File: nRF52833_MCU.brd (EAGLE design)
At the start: 36.3 x 28.4 mm, 20 parts, among them IC1 SKY13415-485LF, IC2 BQ25570RGRR, J100 DEBUG_CONNECTOR, X1 32MHz, X2 32.768kHz

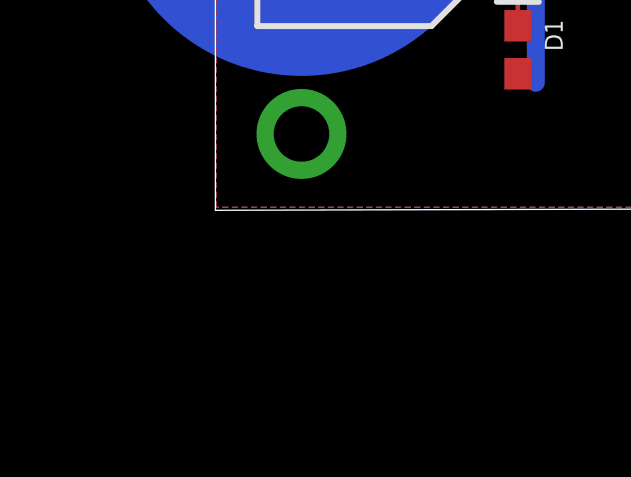
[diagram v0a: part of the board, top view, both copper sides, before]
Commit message: Add gpios for nrf52833
Signed-off-by: Florian Depraz <florian.depraz@outlook.com>
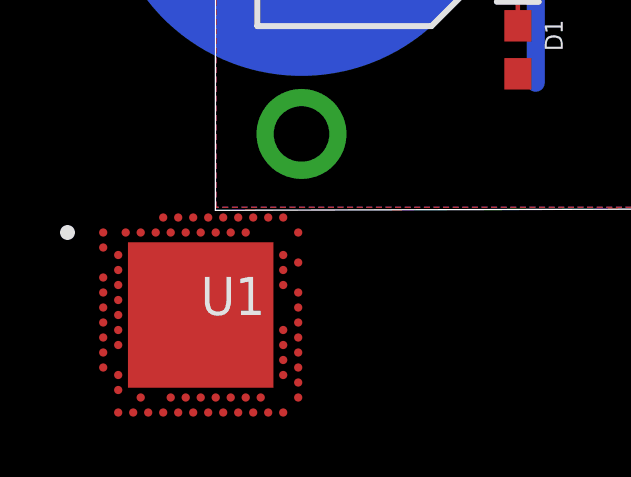
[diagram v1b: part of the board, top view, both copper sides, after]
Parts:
- added U1: nRF52833-QIAA, nrf52833_qiaa:AQFN50P700X700X85_HS-74N
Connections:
- removed net AC31/RESET: J100.10
- removed net P0.19_TX: J100.8
- removed net P0.20_RX: J100.7
- new net DEC1: U1.C1
- new net DEC3: U1.D23
- new net DEC4: U1.B5
- new net DEC5: U1.N24
- new net DEC6: U1.E24
- new net DECUSB: U1.AC5
- new net P0.06_TX: J100.8, U1.L1
- new net P0.07_RX: J100.7, U1.M2
- new net RESET: J100.10, U1.AC13
- new net VBUS: U1.AD2
- new net VDD: U1.A22, U1.AD14, U1.AD23, U1.B1, U1.W1
- new net VDDH: U1.Y2
- new net VSS: U1.74, U1.B7
- new net VSS_PA: U1.F23
- net ANT: now also U1.H23
- net ANT_SEL_V1: now also U1.U24
- net ANT_SEL_V2: now also U1.R24
- net ANT_SEL_V3: now also U1.P23
- net N$3: now also U1.A23
- net N$37: now also U1.B24
- net N$38: now also U1.D2
- net N$39: now also U1.F2
- net P0.21_LED: now also U1.AC17
- net SWDCLK: now also U1.AA24
- net SWDIO: now also U1.AC24
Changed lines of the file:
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@@
 <attribute name="VALUE" x="7.34" y="22.84" size="1.27" layer="27" align="center"/>
+</element>
+<element name="U1" library="nrf52833_qiaa" package="AQFN50P700X700X85_HS-74N" value="nRF52833-QIAA" x="-1.56" y="-3.59" smashed="yes">
+<attribute name="ASSEMBLY" value="" x="-1.56" y="-3.59" size="1.778" layer="27" display="off"/>
+<attribute name="FOOTPRINT_DOC" value="AQFN-73" x="-1.56" y="-3.59" size="1.778" layer="27" display="off"/>
+<attribute name="LATESTREVISIONDATE" value="2018-12-03" x="-1.56" y="-3.59" size="1.778" layer="27" display="off"/>
+<attribute name="MANUFACTURER" value="Nordic Semiconductor" x="-1.56" y="-3.59" size="1.778" layer="27" display="off"/>
+<attribute name="MANUFACTURER_PART_NUMBER" value="nRF52833-QIAA" x="-1.56" y="-3.59" size="1.778" layer="27" display="off"/>
+<attribute name="NAME" x="-1.56" y="-3.59" size="1.27" layer="25" font="vector"/>
+<attribute name="NOTE" value="*" x="-1.56" y="-3.59" size="1.778" layer="27" display="off"/>
+<attribute name="PART_NUMBER" value="nRF52833-QIAA" x="-1.56" y="-3.59" size="1.778" layer="27" display="off"/>
+<attribute name="PIN_COUNT" value="73" x="-1.56" y="-3.59" size="1.778" layer="27" display="off"/>
+<attribute name="PUBLISHED" value="2018-12-03" x="-1.56" y="-3.59" size="1.778" layer="27" display="off"/>
+<attribute name="PUBLISHER" value="Nordic Semiconductor" x="-1.56" y="-3.59" size="1.778" layer="27" display="off"/>
+<attribute name="VALUE" x="-1.56" y="-5.114" size="1.27" layer="27" font="vector"/>
 </element>
 </elements>
@@
 <signal name="ANT">
 <contactref element="IC1" pad="13"/>
-</signal>
-<signal name="P0.19_TX">
+<contactref element="U1" pad="H23"/>
+<wire x1="1.190003125" y1="-2.590003125" x2="18.507" y2="11.12" width="0" layer="19" extent="1-1"/>
+</signal>
+<signal name="P0.06_TX">
 <contactref element="J100" pad="8"/>
+<contactref element="U1" pad="L1"/>
+<wire x1="-4.81" y1="-3.34" x2="1.78" y2="12.31" width="0" layer="19" extent="1-1"/>
 </signal>
 <signal name="P0.21_LED">
 <contactref element="R5" pad="1"/>
-</signal>
-<signal name="P0.20_RX">
+<contactref element="U1" pad="AC17"/>
+<wire x1="-0.56" y1="-6.340003125" x2="9.01" y2="8.6" width="0" layer="19" extent="1-1"/>
+</signal>
+<signal name="P0.07_RX">
 <contactref element="J100" pad="7"/>
-</signal>
-<signal name="AC31/RESET">
-<contactref element="J100" pad="10"/>
+<contactref element="U1" pad="M2"/>
+<wire x1="-4.31" y1="-3.59" x2="5.68" y2="12.31" width="0" layer="19" extent="1-1"/>
 </signal>
 <signal name="SWDCLK">
 <contactref element="J100" pad="4"/>
+<contactref element="U1" pad="AA24"/>
+<wire x1="1.69" y1="-5.84" x2="1.78" y2="9.77" width="0" layer="19" extent="1-1"/>
 </signal>
 <signal name="SWDIO">
 <contactref element="J100" pad="2"/>
+<contactref element="U1" pad="AC24"/>
+<wire x1="1.69" y1="-6.340003125" x2="1.78" y2="8.5" width="0" layer="19" extent="1-1"/>
 </signal>
 <signal name="VDD_P3V3">
@@
 <contactref element="X1" pad="3"/>
 <contactref element="C1" pad="1"/>
+<contactref element="U1" pad="A23"/>
 <wire x1="18.095" y1="16.995" x2="18" y2="18.56" width="0" layer="19" extent="1-1"/>
+<wire x1="1.190003125" y1="-0.34" x2="18.095" y2="16.995" width="0" layer="19" extent="1-1"/>
 </signal>
 <signal name="N$37">
 <contactref element="X1" pad="1"/>
 <contactref element="C5" pad="1"/>
+<contactref element="U1" pad="B24"/>
 <wire x1="17.52" y1="12.73" x2="19.245" y2="15.545" width="0" layer="19" extent="1-1"/>
+<wire x1="1.69" y1="-0.84" x2="17.52" y2="12.73" width="0" layer="19" extent="1-1"/>
 </signal>
 <signal name="N$38">
 <contactref element="X2" pad="1"/>
+<contactref element="U1" pad="D2"/>
+<wire x1="-4.31" y1="-1.59" x2="8.33" y2="12.44" width="0" layer="19" extent="1-1"/>
 </signal>
 <signal name="N$39">
 <contactref element="X2" pad="2"/>
+<contactref element="U1" pad="F2"/>
+<wire x1="-4.31" y1="-2.09" x2="8.33" y2="9.94" width="0" layer="19" extent="1-1"/>
 </signal>
 <signal name="N$5">
@@
 <signal name="ANT_SEL_V1">
 <contactref element="IC1" pad="7"/>
+<contactref element="U1" pad="U24"/>
+<wire x1="1.69" y1="-4.84" x2="20.413" y2="11.52" width="0" layer="19" extent="1-1"/>
 </signal>
 <signal name="ANT_SEL_V2">
 <contactref element="IC1" pad="6"/>
+<contactref element="U1" pad="R24"/>
+<wire x1="1.69" y1="-4.34" x2="20.413" y2="11.12" width="0" layer="19" extent="1-1"/>
 </signal>
 <signal name="ANT_SEL_V3">
 <contactref element="IC1" pad="5"/>
+<contactref element="U1" pad="P23"/>
+<wire x1="1.190003125" y1="-4.09" x2="20.413" y2="10.72" width="0" layer="19" extent="1-1"/>
 </signal>
 <signal name="ANT_OUT_RF1">
@@
 <via x="25.5" y="22.37" extent="1-16" drill="0.4"/>
 </signal>
+<signal name="VSS">
+<contactref element="U1" pad="74"/>
+<contactref element="U1" pad="B7"/>
+<wire x1="-3.06" y1="-0.84" x2="-1.56" y2="-3.59" width="0" layer="19" extent="1-1"/>
+</signal>
+<signal name="VDD">
+<contactref element="U1" pad="AD14"/>
+<contactref element="U1" pad="AD23"/>
+<contactref element="U1" pad="B1"/>
+<contactref element="U1" pad="A22"/>
+<contactref element="U1" pad="W1"/>
+<wire x1="-1.309996875" y1="-6.84" x2="-4.81" y2="-5.340003125" width="0" layer="19" extent="1-1"/>
+<wire x1="1.190003125" y1="-6.84" x2="-1.309996875" y2="-6.84" width="0" layer="19" extent="1-1"/>
+<wire x1="-4.81" y1="-0.84" x2="-4.81" y2="-5.340003125" width="0" layer="19" extent="1-1"/>
+<wire x1="0.690003125" y1="-0.34" x2="-4.81" y2="-0.84" width="0" layer="19" extent="1-1"/>
+</signal>
+<signal name="DEC5">
+<contactref element="U1" pad="N24"/>
+</signal>
+<signal name="DECUSB">
+<contactref element="U1" pad="AC5"/>
+</signal>
+<signal name="VBUS">
+<contactref element="U1" pad="AD2"/>
+</signal>
+<signal name="VDDH">
+<contactref element="U1" pad="Y2"/>
+</signal>
+<signal name="DEC4">
+<contactref element="U1" pad="B5"/>
+</signal>
+<signal name="DEC3">
+<contactref element="U1" pad="D23"/>
+</signal>
+<signal name="DEC6">
+<contactref element="U1" pad="E24"/>
+</signal>
+<signal name="VSS_PA">
+<contactref element="U1" pad="F23"/>
+</signal>
+<signal name="RESET">
+<contactref element="U1" pad="AC13"/>
+<contactref element="J100" pad="10"/>
+<wire x1="-1.56" y1="-6.340003125" x2="1.78" y2="13.58" width="0" layer="19" extent="1-1"/>
+</signal>
+<signal name="DEC1">
+<contactref element="U1" pad="C1"/>
+</signal>
 </signals>

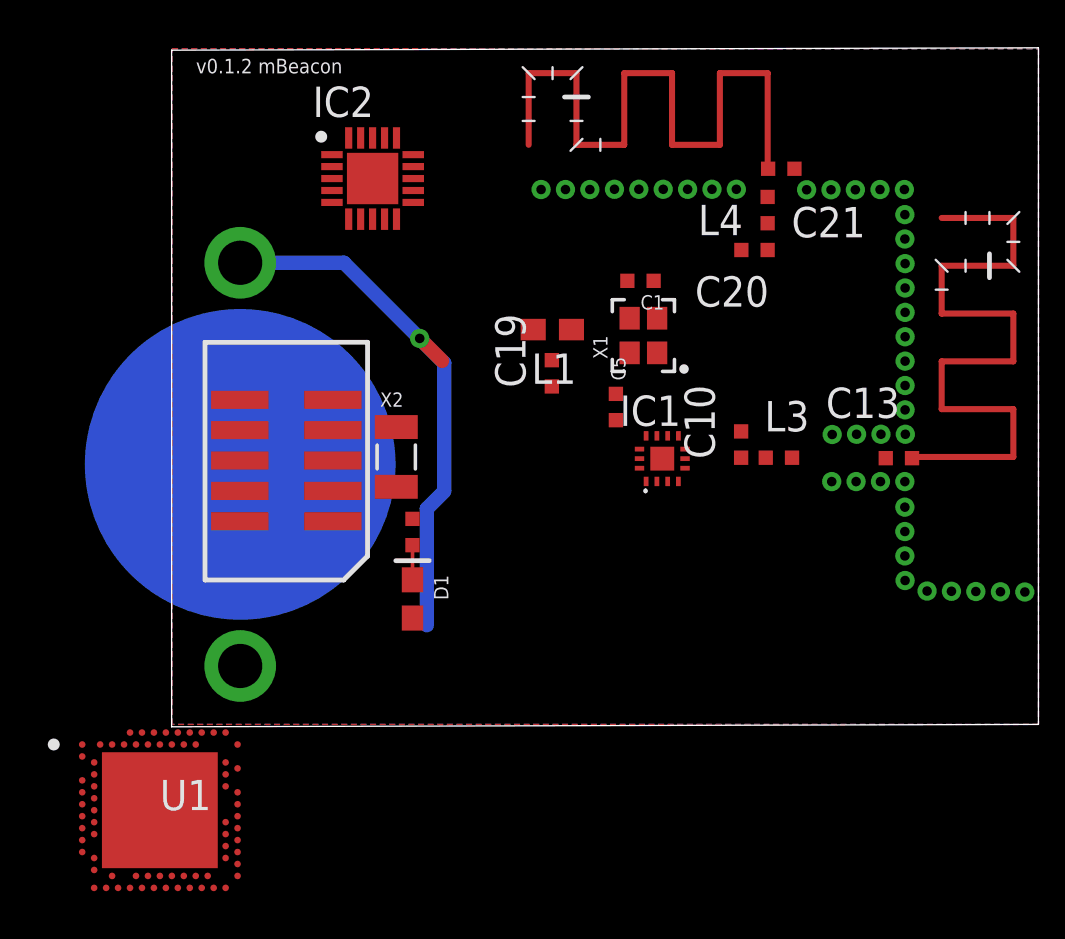
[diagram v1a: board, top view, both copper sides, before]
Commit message: Add capa for option 3 nrf52833
Signed-off-by: Florian Depraz <florian.depraz@outlook.com>
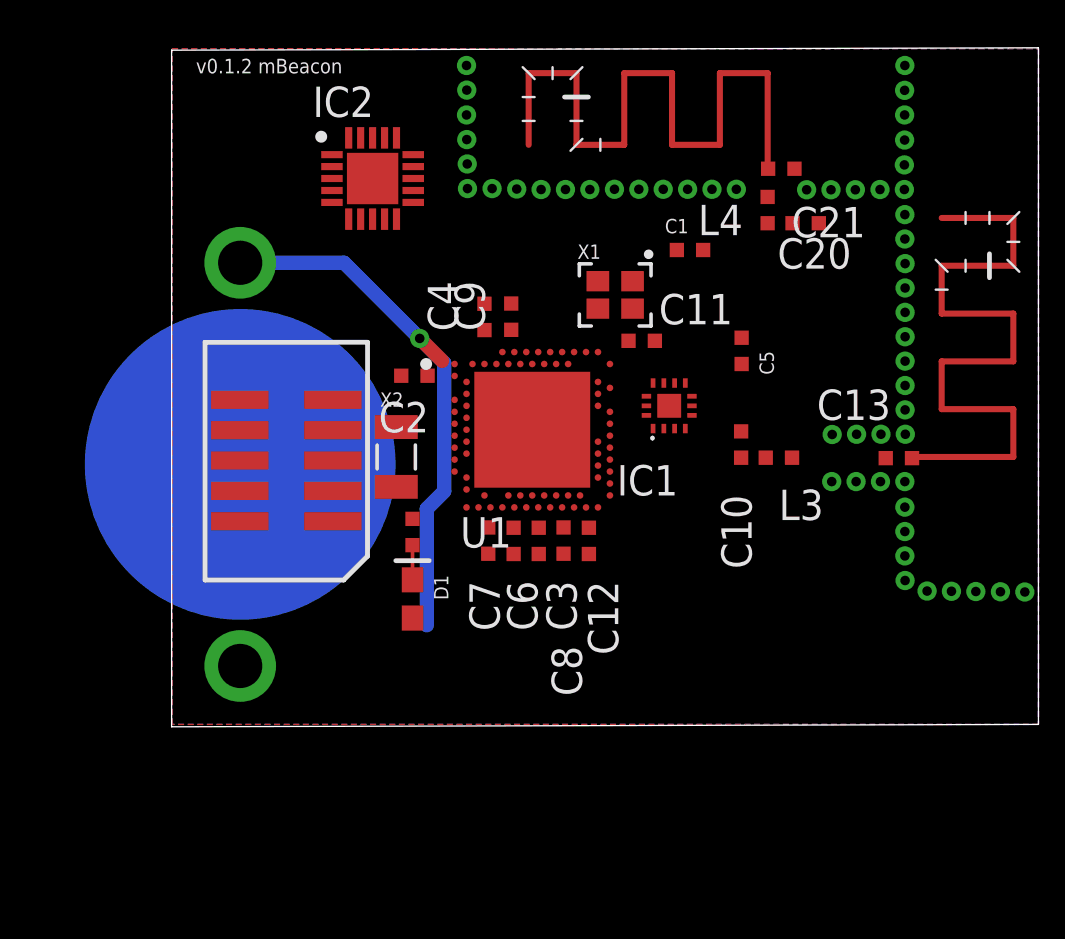
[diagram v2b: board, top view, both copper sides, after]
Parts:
- removed C19: 100nF, Nordic_misc:RESC0402_N
- removed L1: 10µH, Nordic_misc:RESC0603_N
- added C11: 100pF, Nordic_misc:RESC0402_N
- added C12, C2, C7, C8: 100nF, Nordic_misc:RESC0402_N
- added C3, C4: 1.0uF, Nordic_misc:RESC0402_N
- added C6: 4.7uF, Nordic_misc:RESC0402_N
- added C9: NC, Nordic_misc:RESC0402_N
- moved U1 22.3 mm to (14.0, 12.3)
- moved C5 5.76 mm to (22.8, 15.6)
- moved C1 2.44 mm to (20.6, 19.9)
- moved C20 2.42 mm to (25.5, 21.0), turned to 0 degrees
- moved IC1 2.23 mm to (19.8, 13.3)
- moved X1 2.07 mm to (17.5, 18.0), turned to 180 degrees
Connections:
- removed net DEC1: U1.C1
- removed net DEC3: U1.D23
- removed net DEC4: U1.B5
- removed net DEC6: U1.E24
- removed net N$36: C19.1
- removed net VDD: U1.A22, U1.AD14, U1.AD23, U1.B1, U1.W1
- removed net VDDH: U1.Y2
- new net N$18: C12.1, C3.1, C6.1, C7.1, C8.1, U1.A22, U1.AD14, U1.AD23, U1.B1, U1.W1, U1.Y2
- new net N$19: C4.1, C9.1, U1.B5, U1.E24
- new net N$2: C2.1, U1.C1
- new net N$21: C11.1, U1.D23
- net GND: now also C11.2, C12.2, C2.2, C3.2, C4.2, C6.2, C7.2, C8.2, C9.2, U1.74; no longer C19.2
- net VSS: no longer U1.74

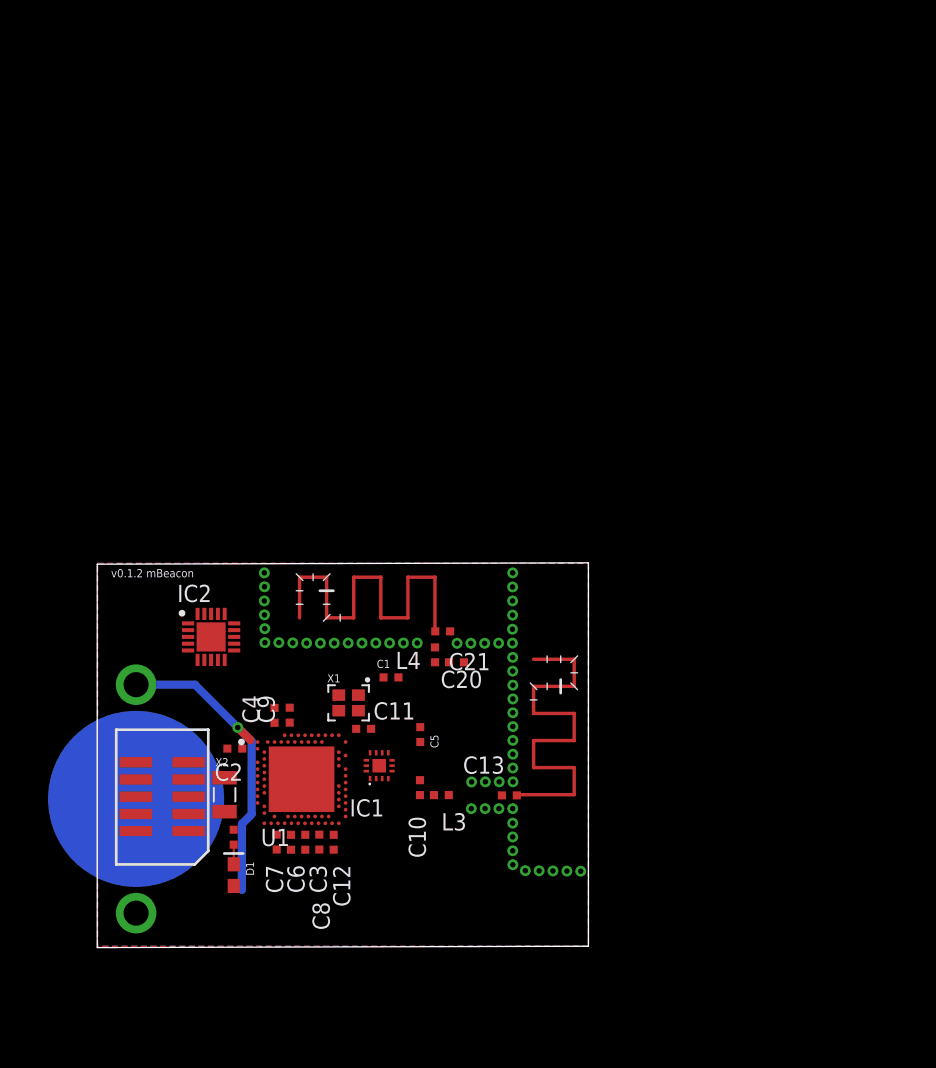
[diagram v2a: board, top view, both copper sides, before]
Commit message: Redefine schematic to add energy harvest
Signed-off-by: Florian Depraz <florian.depraz@outlook.com>
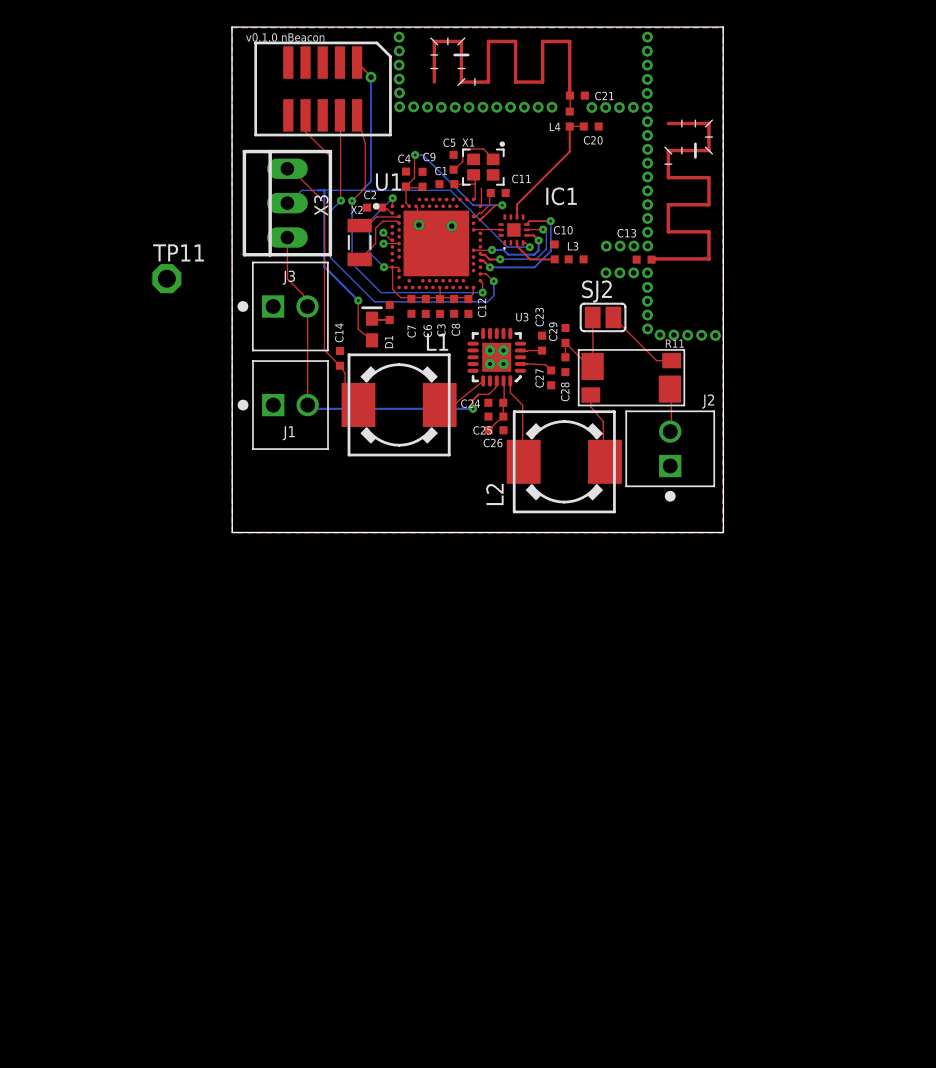
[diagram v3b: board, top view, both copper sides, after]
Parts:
- removed BATT1: CR1632, Nordic_misc:CR1632_HOLDER_TH
- removed IC2: BQ25570RGRR, SamacSys_Parts:QFN50P350X350X100-21N
- added C14, C26, C29: NC, Nordic_misc:RESC0402_N
- added C23: 0.01uF, Nordic_misc:RESC0402_N
- added C24, C27: 0.1uF, Nordic_misc:RESC0402_N
- added C25, C28: 4.7uF, Nordic_misc:RESC0402_N
- added J1, J2, J3: 282834-2, 282834-2:CONN_282834-2
- added L1, L2: DR73-220-R, DR73-220-R:DR73
- added R11: 0.05R, Y14870RXX000B9R:Y14870RXX000B9R
- added SJ2: (no value), jumper:SJ
- added TP11: TPPAD1-13, testpad:P1-13
- added U3: BQ25570RGRR, BQ25570RGRR:QFN50P350X350X100-21N
- added X3: 22-23-2031, con-molex:22-23-2031
- moved J100 53.6 mm to (15.6, 63.3), turned to 180 degrees
- moved C5 42.3 mm to (25.2, 57.9)
- moved X2 42.0 mm to (18.3, 52.0)
- moved D1 41.6 mm to (19.2, 45.5)
- moved C2 41.3 mm to (19.4, 54.5)
- moved C11 40.8 mm to (28.5, 55.6)
- moved ANT1 40.8 mm to (40.1, 50.8)
- moved ANT2 40.8 mm to (33.8, 62.8)
- moved C10 40.8 mm to (32.7, 51.3)
- moved C12 40.8 mm to (26.3, 47.2)
- moved C13 40.8 mm to (39.3, 50.7)
- moved C20 40.8 mm to (35.4, 60.5)
- moved C21 40.8 mm to (34.4, 62.8)
- moved C3 40.8 mm to (24.2, 47.2)
- moved C6 40.8 mm to (23.2, 47.2)
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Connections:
- net N$18 renamed VDD
- net N$19 renamed DEC6
- net N$2 renamed DEC1
- net N$21 renamed DEC3
- net N$3 renamed XC2
- net N$37 renamed XC1
- net N$38 renamed XL1
- net N$39 renamed XL2
- new net BQ_LBUCK: L1.2, U3.16
- new net BQ_NEN: U3.5
- new net BQ_OK_HYST: U3.10
- new net BQ_OK_PROG: U3.11
- new net BQ_RSP1: J2.2, R11.P$3, R11.P$4, SJ2.2
- new net BQ_SUPPLY_VBAT: C14.1, L1.1, X3.3
- new net BQ_VBAT_OK: U3.13
- new net BQ_VBAT_OV: U3.7
- new net BQ_VIN_DC: C27.1, C28.1, C29.1, L2.1, R11.P$1, R11.P$2, SJ2.1, U3.2
- new net BQ_VOUT: U3.14
- new net BQ_VOUT_EN: U3.6
- new net BQ_VOUT_SET: U3.12
- new net BQ_VRDIV: U3.8
- new net BQ_VSTOR: C24.1, C25.1, C26.1, U3.19
- new net EXT_VBAT: J1.2, J3.2, U3.18, X3.1
- new net LBOOST: L2.2, U3.20
- new net VOC_SAMP: U3.3
- new net VREF_SAMP: C23.1, U3.4
- net GND: now also C14.2, C23.2, C24.2, C25.2, C26.2, C27.2, C28.2, C29.2, J1.1, J2.1, J3.1, U3.1, U3.15, U3.17, U3.21, U3.22, U3.23, U3.24, U3.25, U3.9; no longer BATT1.1, C3.2, U1.74
- net VDD_P3V3: now also IC1.4, X3.2; no longer BATT1.2
- net VSS: now also C3.2, U1.74
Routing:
- net EXT_VBAT: track 0.00 -> 28.6 mm, vias 0 -> 1
- net SWDCLK: track 0.00 -> 26.7 mm, vias 0 -> 2
- net SWDIO: track 0.00 -> 22.9 mm, vias 0 -> 2
- net VDD_P3V3: track 23.2 -> 44.2 mm, vias 1 -> 3
- net BQ_SUPPLY_VBAT: track 0.00 -> 19.9 mm
- net VDD: track 0.00 -> 17.8 mm, vias 0 -> 2
- net BQ_VIN_DC: track 0.00 -> 16.5 mm
- net DEC6: track 0.00 -> 15.6 mm, vias 0 -> 2
- net ANT_SEL_V1: track 0.00 -> 10.3 mm, vias 0 -> 2
- net ANT_OUT_RF2: track 0.00 -> 9.34 mm
- net BQ_RSP1: track 0.00 -> 8.89 mm
- net ANT_SEL_V2: track 0.00 -> 8.11 mm, vias 0 -> 2
- net ANT_SEL_V3: track 0.00 -> 6.82 mm, vias 0 -> 2
- net LBOOST: track 0.00 -> 6.39 mm
- net XC1: track 0.00 -> 5.69 mm
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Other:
- board size 36.3 x 28.4 mm -> 36.3 x 37.3 mm
- board text added: "v0.1.0 nBeacon"
- board text removed: "v0.1.2 mBeacon"
